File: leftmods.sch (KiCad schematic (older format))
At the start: 13 parts

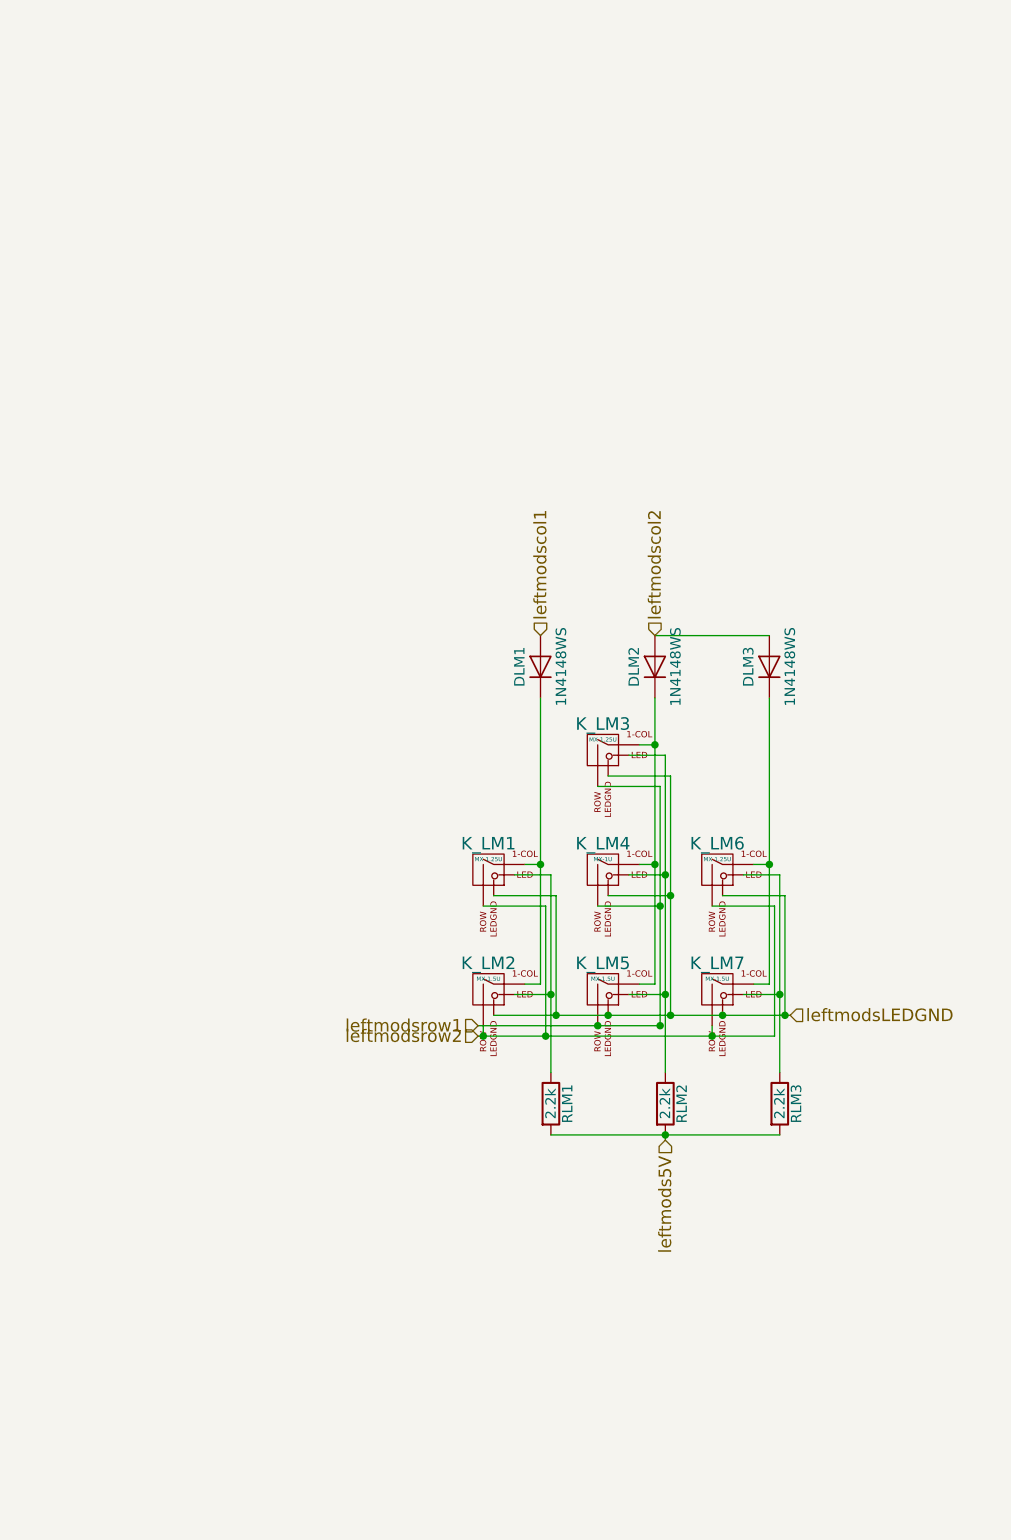
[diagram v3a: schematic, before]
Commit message: more left mods added
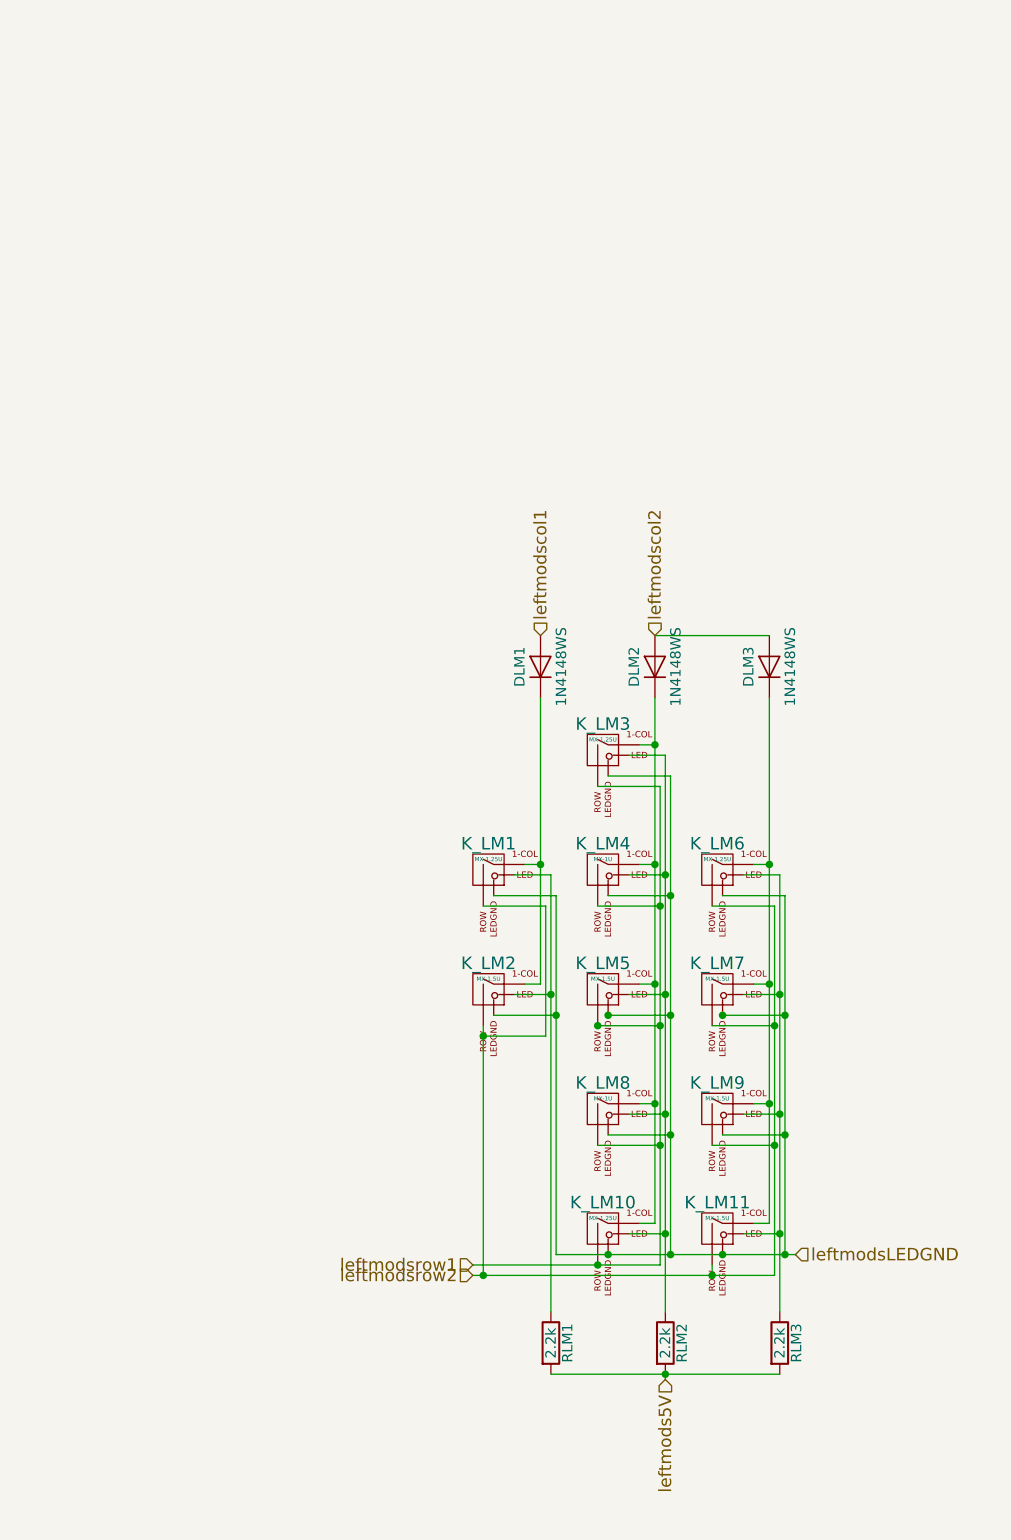
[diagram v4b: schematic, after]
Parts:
- added K_LM10: MX-1.25U, MX_Alps_Hybrid:MX-1.25U, symbol MX-1.25U
- added K_LM11, K_LM9: MX-1.5U, MX_Alps_Hybrid:MX-1.5U, symbol MX-1.5U
- added K_LM8: MX-1U, MX_Alps_Hybrid:MX-1U, symbol MX-1U
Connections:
- net leftmodsLEDGND: now also K_LM10.4 (LEDGND), K_LM11.4 (LEDGND), K_LM8.4 (LEDGND), K_LM9.4 (LEDGND)
- net leftmodsrow1: now also K_LM10.2 (ROW), K_LM8.2 (ROW)
- net leftmodsrow2: now also K_LM11.2 (ROW), K_LM9.2 (ROW)
- net at DLM2.1 (K), K_LM3.1 (COL), K_LM4.1 (COL)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: now also K_LM10.1 (COL), K_LM8.1 (COL)
- net at K_LM3.3 (LED), K_LM4.3 (LED), K_LM5.3 (LED)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: now also K_LM10.3 (LED), K_LM8.3 (LED)
- net at DLM3.1 (K), K_LM6.1 (COL), K_LM7.1 (COL): now also K_LM11.1 (COL), K_LM9.1 (COL)
- net at K_LM6.3 (LED), K_LM7.3 (LED), RLM3.1: now also K_LM11.3 (LED), K_LM9.3 (LED)
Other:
- moved on the sheet: RLM1, RLM2, RLM3
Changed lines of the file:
@@
 	1    0    0    -1
 $EndComp
-Text HLabel 4200 5450 0    60   Input ~ 0
+Text HLabel 4175 6600 0    60   Input ~ 0
 leftmodsrow1
 $Comp
@@
 L R RLM1
 U 1 1 591D3F53
-P 4550 5825
-F 0 "RLM1" V 4630 5825 50  0000 C CNN
-F 1 "2.2k" V 4550 5825 50  0000 C CNN
-F 2 "" V 4480 5825 50  0001 C CNN
-F 3 "" H 4550 5825 50  0000 C CNN
-	1    4550 5825
+P 4550 6975
+F 0 "RLM1" V 4630 6975 50  0000 C CNN
+F 1 "2.2k" V 4550 6975 50  0000 C CNN
+F 2 "" V 4480 6975 50  0001 C CNN
+F 3 "" H 4550 6975 50  0000 C CNN
+	1    4550 6975
 	1    0    0    -1
 $EndComp
@@
 L R RLM2
 U 1 1 591D4076
-P 5100 5825
-F 0 "RLM2" V 5180 5825 50  0000 C CNN
-F 1 "2.2k" V 5100 5825 50  0000 C CNN
-F 2 "" V 5030 5825 50  0001 C CNN
-F 3 "" H 5100 5825 50  0000 C CNN
-	1    5100 5825
+P 5100 6975
+F 0 "RLM2" V 5180 6975 50  0000 C CNN
+F 1 "2.2k" V 5100 6975 50  0000 C CNN
+F 2 "" V 5030 6975 50  0001 C CNN
+F 3 "" H 5100 6975 50  0000 C CNN
+	1    5100 6975
 	1    0    0    -1
 $EndComp
@@
 L R RLM3
 U 1 1 591D444F
-P 5650 5825
-F 0 "RLM3" V 5730 5825 50  0000 C CNN
-F 1 "2.2k" V 5650 5825 50  0000 C CNN
-F 2 "" V 5580 5825 50  0001 C CNN
-F 3 "" H 5650 5825 50  0000 C CNN
-	1    5650 5825
-	1    0    0    -1
-$EndComp
-Text HLabel 5700 5400 2    60   Input ~ 0
+P 5650 6975
+F 0 "RLM3" V 5730 6975 50  0000 C CNN
+F 1 "2.2k" V 5650 6975 50  0000 C CNN
+F 2 "" V 5580 6975 50  0001 C CNN
+F 3 "" H 5650 6975 50  0000 C CNN
+	1    5650 6975
+	1    0    0    -1
+$EndComp
+Text HLabel 5725 6550 2    60   Input ~ 0
 leftmodsLEDGND
-Text HLabel 5100 6000 3    60   Input ~ 0
+Text HLabel 5100 7150 3    60   Input ~ 0
 leftmods5V
-Text HLabel 4200 5500 0    60   Input ~ 0
+Text HLabel 4175 6650 0    60   Input ~ 0
 leftmodsrow2
-Wire Wire Line
-	4975 4100 5050 4100
-Wire Wire Line
-	5050 3875 5050 5250
-Wire Wire Line
-	5050 4675 4975 4675
-Wire Wire Line
-	5050 5250 4975 5250
-Connection ~ 5050 4675
-Wire Wire Line
-	5525 4675 5600 4675
-Wire Wire Line
-	5600 3875 5600 5250
-Wire Wire Line
-	5600 5250 5525 5250
-Wire Wire Line
-	4425 4675 4500 4675
-Wire Wire Line
-	4500 3875 4500 5250
-Wire Wire Line
-	4500 5250 4425 5250
-Wire Wire Line
-	4775 4300 5075 4300
-Wire Wire Line
-	5075 4300 5075 5450
-Wire Wire Line
-	5075 4875 4775 4875
-Wire Wire Line
-	5075 5450 4200 5450
-Connection ~ 5075 4875
-Wire Wire Line
-	4225 4875 4525 4875
-Connection ~ 4775 5450
-Wire Wire Line
-	5325 4875 5625 4875
-Wire Wire Line
-	5625 4875 5625 5500
-Connection ~ 5075 5450
-Wire Wire Line
-	4375 4725 4550 4725
-Wire Wire Line
-	4550 4725 4550 5675
-Wire Wire Line
-	4550 5300 4375 5300
-Wire Wire Line
-	4275 5400 5700 5400
-Wire Wire Line
-	4575 5400 4575 4825
-Wire Wire Line
-	4575 4825 4275 4825
-Connection ~ 4575 5400
-Wire Wire Line
-	4925 4725 5100 4725
-Wire Wire Line
-	5100 4150 5100 5675
-Wire Wire Line
-	5100 5300 4925 5300
-Wire Wire Line
-	4925 4150 5100 4150
-Connection ~ 5100 4725
-Wire Wire Line
-	4825 4825 5125 4825
-Wire Wire Line
-	5125 4250 5125 5400
-Connection ~ 4825 5400
-Wire Wire Line
-	4825 4250 5125 4250
-Connection ~ 5125 4825
-Wire Wire Line
-	5475 4725 5650 4725
-Wire Wire Line
-	5650 4725 5650 5675
-Wire Wire Line
-	5650 5300 5475 5300
-Connection ~ 5125 5400
-Wire Wire Line
-	5675 5400 5675 4825
-Wire Wire Line
-	5675 4825 5375 4825
-Connection ~ 5375 5400
-Connection ~ 4500 4675
-Connection ~ 5050 4100
-Connection ~ 5600 4675
-Connection ~ 4550 5300
-Connection ~ 5100 5300
-Connection ~ 5650 5300
-Wire Wire Line
-	4550 5975 5650 5975
-Connection ~ 5100 5975
-Connection ~ 5675 5400
-Wire Wire Line
-	5100 6000 5100 5975
-Wire Wire Line
-	5625 5500 4200 5500
-Wire Wire Line
-	4225 5500 4225 5450
-Wire Wire Line
-	4525 4875 4525 5500
-Connection ~ 4225 5500
-Wire Wire Line
-	5325 5500 5325 5450
-Connection ~ 4525 5500
-Connection ~ 5325 5500
-Wire Wire Line
-	5050 3575 5600 3575
 $Comp
 L MX-1.25U K_LM3
@@
 	1    0    0    -1
 $EndComp
+$Comp
+L MX-1U K_LM8
+U 1 1 594A5358
+P 4800 5850
+F 0 "K_LM8" H 4800 5975 60  0000 C CNN
+F 1 "MX-1U" H 4800 5900 20  0000 C CNN
+F 2 "MX_Alps_Hybrid:MX-1U" H 4775 5825 60  0001 C CNN
+F 3 "" H 4775 5825 60  0001 C CNN
+	1    4800 5850
+	1    0    0    -1
+$EndComp
+$Comp
+L MX-1.5U K_LM9
+U 1 1 594A64BB
+P 5350 5850
+F 0 "K_LM9" H 5350 5975 60  0000 C CNN
+F 1 "MX-1.5U" H 5350 5900 20  0000 C CNN
+F 2 "MX_Alps_Hybrid:MX-1.5U" H 5325 5825 60  0001 C CNN
+F 3 "" H 5325 5825 60  0001 C CNN
+	1    5350 5850
+	1    0    0    -1
+$EndComp
+$Comp
+L MX-1.5U K_LM11
+U 1 1 594A6C8D
+P 5350 6425
+F 0 "K_LM11" H 5350 6550 60  0000 C CNN
+F 1 "MX-1.5U" H 5350 6475 20  0000 C CNN
+F 2 "MX_Alps_Hybrid:MX-1.5U" H 5325 6400 60  0001 C CNN
+F 3 "" H 5325 6400 60  0001 C CNN
+	1    5350 6425
+	1    0    0    -1
+$EndComp
+$Comp
+L MX-1.25U K_LM10
+U 1 1 594A6D23
+P 4800 6425
+F 0 "K_LM10" H 4800 6550 60  0000 C CNN
+F 1 "MX-1.25U" H 4800 6475 20  0000 C CNN
+F 2 "MX_Alps_Hybrid:MX-1.25U" H 4775 6400 60  0001 C CNN
+F 3 "" H 4775 6400 60  0001 C CNN
+	1    4800 6425
+	1    0    0    -1
+$EndComp
+Connection ~ 5050 5250
+Wire Wire Line
+	5050 5825 4975 5825
+Wire Wire Line
+	5100 5875 4925 5875
+Wire Wire Line
+	5075 6025 4775 6025
+Wire Wire Line
+	5125 5975 4825 5975
+Wire Wire Line
+	5125 5400 4825 5400
+Wire Wire Line
+	5050 3575 5600 3575
+Connection ~ 4225 5500
+Wire Wire Line
+	4525 4875 4525 5500
+Wire Wire Line
+	4225 5450 4225 6650
+Wire Wire Line
+	4525 5500 4225 5500
+Wire Wire Line
+	5100 7150 5100 7125
+Connection ~ 5675 5400
+Connection ~ 5100 7125
+Wire Wire Line
+	4550 7125 5650 7125
+Connection ~ 5650 5300
+Connection ~ 5100 5300
+Connection ~ 4550 5300
+Connection ~ 5600 4675
+Connection ~ 5050 4100
+Connection ~ 4500 4675
+Connection ~ 5375 5400
+Wire Wire Line
+	5675 4825 5375 4825
+Wire Wire Line
+	5675 6550 5675 4825
+Connection ~ 5125 5400
+Wire Wire Line
+	5650 5300 5475 5300
+Wire Wire Line
+	5650 4725 5650 6825
+Wire Wire Line
+	5475 4725 5650 4725
+Connection ~ 5125 4825
+Wire Wire Line
+	4825 4250 5125 4250
+Connection ~ 4825 5400
+Wire Wire Line
+	5125 4250 5125 6550
+Wire Wire Line
+	4825 4825 5125 4825
+Connection ~ 5100 4725
+Wire Wire Line
+	4925 4150 5100 4150
+Wire Wire Line
+	5100 5300 4925 5300
+Wire Wire Line
+	5100 4150 5100 6825
+Wire Wire Line
+	4925 4725 5100 4725
+Connection ~ 4575 5400
+Wire Wire Line
+	4575 4825 4275 4825
+Wire Wire Line
+	4575 4825 4575 6550
+Wire Wire Line
+	5375 5400 5675 5400
+Wire Wire Line
+	4275 5400 4575 5400
+Wire Wire Line
+	4550 5300 4375 5300
+Wire Wire Line
+	4550 4725 4550 6825
+Wire Wire Line
+	4375 4725 4550 4725
+Connection ~ 5075 5450
+Wire Wire Line
+	5625 6650 5625 4875
+Wire Wire Line
+	5625 4875 5325 4875
+Connection ~ 4775 5450
+Wire Wire Line
+	4225 4875 4525 4875
+Connection ~ 5075 4875
+Wire Wire Line
+	5075 5450 4775 5450
+Wire Wire Line
+	5075 4875 4775 4875
+Wire Wire Line
+	5075 6600 5075 4300
+Wire Wire Line
+	5075 4300 4775 4300
+Wire Wire Line
+	4500 5250 4425 5250
+Wire Wire Line
+	4500 3875 4500 5250
+Wire Wire Line
+	4425 4675 4500 4675
+Wire Wire Line
+	5600 5250 5525 5250
+Wire Wire Line
+	5600 3875 5600 6400
+Wire Wire Line
+	5525 4675 5600 4675
+Connection ~ 5050 4675
+Wire Wire Line
+	5050 5250 4975 5250
+Wire Wire Line
+	5050 4675 4975 4675
+Wire Wire Line
+	5050 3875 5050 6400
+Wire Wire Line
+	4975 4100 5050 4100
+Wire Wire Line
+	5325 6650 5325 6600
+Wire Wire Line
+	4175 6650 5625 6650
+Connection ~ 4225 6650
+Wire Wire Line
+	4175 6600 5075 6600
+Connection ~ 5075 6025
+Connection ~ 4775 6600
+Wire Wire Line
+	5325 5450 5625 5450
+Connection ~ 5625 5450
+Connection ~ 5325 6650
+Wire Wire Line
+	4575 6550 5725 6550
+Connection ~ 5125 5975
+Wire Wire Line
+	5100 6450 4925 6450
+Connection ~ 5100 5875
+Wire Wire Line
+	5050 6400 4975 6400
+Connection ~ 5050 5825
+Wire Wire Line
+	5600 5825 5525 5825
+Connection ~ 5600 5250
+Wire Wire Line
+	5600 6400 5525 6400
+Connection ~ 5600 5825
+Wire Wire Line
+	5650 5875 5475 5875
+Wire Wire Line
+	5650 6450 5475 6450
+Connection ~ 5650 5875
+Connection ~ 5100 6450
+Connection ~ 5650 6450
+Connection ~ 4825 6550
+Connection ~ 5375 6550
+Connection ~ 5125 6550
+Connection ~ 5675 6550
+Wire Wire Line
+	5325 6025 5625 6025
+Connection ~ 5625 6025
+Wire Wire Line
+	5375 5975 5675 5975
+Connection ~ 5675 5975
 $EndSCHEMATC

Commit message: Fix left mods diode location
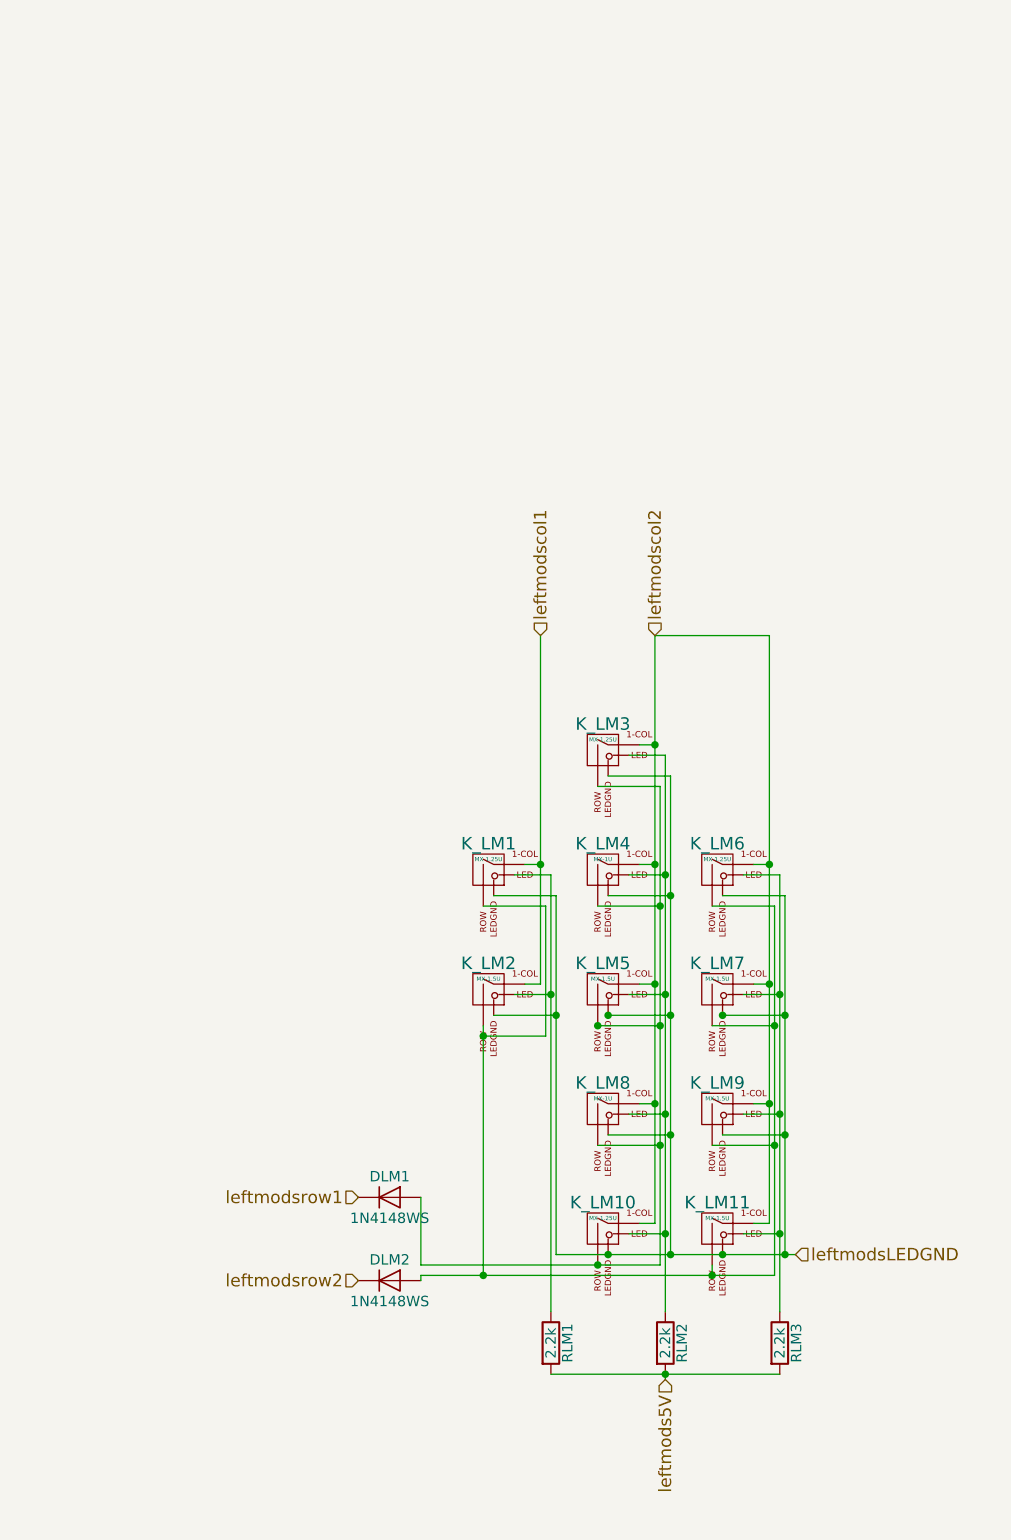
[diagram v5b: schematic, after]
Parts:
- removed DLM3: 1N4148WS, symbol D
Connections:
- net leftmodscol1: now also K_LM1.1 (COL), K_LM2.1 (COL); no longer DLM1.2 (A)
- net leftmodscol2: now also K_LM10.1 (COL), K_LM11.1 (COL), K_LM3.1 (COL), K_LM4.1 (COL), K_LM5.1 (COL), K_LM6.1 (COL), K_LM7.1 (COL), K_LM8.1 (COL), K_LM9.1 (COL); no longer DLM2.2 (A)
- net leftmodsrow1: now also DLM1.1 (K); no longer K_LM10.2 (ROW), K_LM3.2 (ROW), K_LM4.2 (ROW), K_LM5.2 (ROW), K_LM8.2 (ROW)
- net leftmodsrow2: now also DLM2.1 (K); no longer K_LM1.2 (ROW), K_LM11.2 (ROW), K_LM2.2 (ROW), K_LM6.2 (ROW), K_LM7.2 (ROW), K_LM9.2 (ROW)
- new net: DLM2.2 (A), K_LM1.2 (ROW), K_LM11.2 (ROW), K_LM2.2 (ROW), K_LM6.2 (ROW), K_LM7.2 (ROW), K_LM9.2 (ROW)
- new net: DLM1.2 (A), K_LM10.2 (ROW), K_LM3.2 (ROW), K_LM4.2 (ROW), K_LM5.2 (ROW), K_LM8.2 (ROW)
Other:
- moved on the sheet: DLM1, DLM2
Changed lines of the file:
@@
 	1    0    0    -1
 $EndComp
-Text HLabel 4175 6600 0    60   Input ~ 0
+Text HLabel 3625 6275 0    60   Input ~ 0
 leftmodsrow1
 $Comp
 L D DLM1
 U 1 1 591D216C
-P 4500 3725
-F 0 "DLM1" H 4500 3825 50  0000 C CNN
-F 1 "1N4148WS" H 4500 3625 50  0000 C CNN
-F 2 "" H 4500 3725 50  0001 C CNN
-F 3 "" H 4500 3725 50  0000 C CNN
-	1    4500 3725
-	0    -1   -1   0
+P 3775 6275
+F 0 "DLM1" H 3775 6375 50  0000 C CNN
+F 1 "1N4148WS" H 3775 6175 50  0000 C CNN
+F 2 "" H 3775 6275 50  0001 C CNN
+F 3 "" H 3775 6275 50  0000 C CNN
+	1    3775 6275
+	1    0    0    -1
 $EndComp
 $Comp
 L D DLM2
 U 1 1 591D28A1
-P 5050 3725
-F 0 "DLM2" H 5050 3825 50  0000 C CNN
-F 1 "1N4148WS" H 5050 3625 50  0000 C CNN
-F 2 "" H 5050 3725 50  0001 C CNN
-F 3 "" H 5050 3725 50  0000 C CNN
-	1    5050 3725
-	0    -1   -1   0
-$EndComp
-$Comp
-L D DLM3
-U 1 1 591D2AA8
-P 5600 3725
-F 0 "DLM3" H 5600 3825 50  0000 C CNN
-F 1 "1N4148WS" H 5600 3625 50  0000 C CNN
-F 2 "" H 5600 3725 50  0001 C CNN
-F 3 "" H 5600 3725 50  0000 C CNN
-	1    5600 3725
-	0    -1   -1   0
+P 3775 6675
+F 0 "DLM2" H 3775 6775 50  0000 C CNN
+F 1 "1N4148WS" H 3775 6575 50  0000 C CNN
+F 2 "" H 3775 6675 50  0001 C CNN
+F 3 "" H 3775 6675 50  0000 C CNN
+	1    3775 6675
+	1    0    0    -1
 $EndComp
 Text HLabel 4500 3575 1    60   Input ~ 0
@@
 Text HLabel 5100 7150 3    60   Input ~ 0
 leftmods5V
-Text HLabel 4175 6650 0    60   Input ~ 0
+Text HLabel 3625 6675 0    60   Input ~ 0
 leftmodsrow2
 $Comp
@@
 	4500 5250 4425 5250
 Wire Wire Line
-	4500 3875 4500 5250
+	4500 3575 4500 5250
 Wire Wire Line
 	4425 4675 4500 4675
@@
 	5600 5250 5525 5250
 Wire Wire Line
-	5600 3875 5600 6400
+	5600 3575 5600 6400
 Wire Wire Line
 	5525 4675 5600 4675
@@
 	5050 4675 4975 4675
 Wire Wire Line
-	5050 3875 5050 6400
+	5050 3575 5050 6400
 Wire Wire Line
 	4975 4100 5050 4100
@@
 	5325 6650 5325 6600
 Wire Wire Line
-	4175 6650 5625 6650
+	3925 6650 5625 6650
 Connection ~ 4225 6650
 Wire Wire Line
-	4175 6600 5075 6600
+	3925 6600 5075 6600
 Connection ~ 5075 6025
 Connection ~ 4775 6600
@@
 	5375 5975 5675 5975
 Connection ~ 5675 5975
+Wire Wire Line
+	3925 6275 3925 6600
+Wire Wire Line
+	3925 6675 3925 6650
 $EndSCHEMATC
